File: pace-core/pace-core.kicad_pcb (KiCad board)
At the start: 4 copper layers, 100 x 80.1 mm, 174 parts, among them CN1 XT60PW-M, CN2 SMTSOM330BTR, CN3 SMTSOM330BTR, CN4 SMTSOM330BTR, CN5 SMTSOM330BTR, CN6 SMTSOM330BTR, CN7 SMTSOM330BTR, J1 MotorOut, J2 Wiz5500-Coprocessor-BoB, J4 Conn_02x05_Odd_Even, Q1 BSS138, Q10 ISC0802NLSATMA1, Q11 ISC0802NLSATMA1, Q12 ISC0802NLSATMA1, Q2 BSS138, Q3 BSS138, Q7 ISC0802NLSATMA1, Q8 ISC0802NLSATMA1, Q9 ISC0802NLSATMA1, SW1 SKRPACE010, SW2 SKRPACE010, SW3 DPDT, U1 ESP32-S3-WROOM-1, U10 LM75ADP,118, U11 LM75ADP,118, U12 SM06B-SRSS-TB, U13 SM06B-SRSS-TB, U2 DRV8353SRTAT, U3 USBLC6-2P6, U4 ADUM3160BRWZ-RL, U5 AMS1117-3.3, U6 XL7015E1, U7 REF35160QDBVR, U8 LM75ADP,118, U9 LM75ADP,118

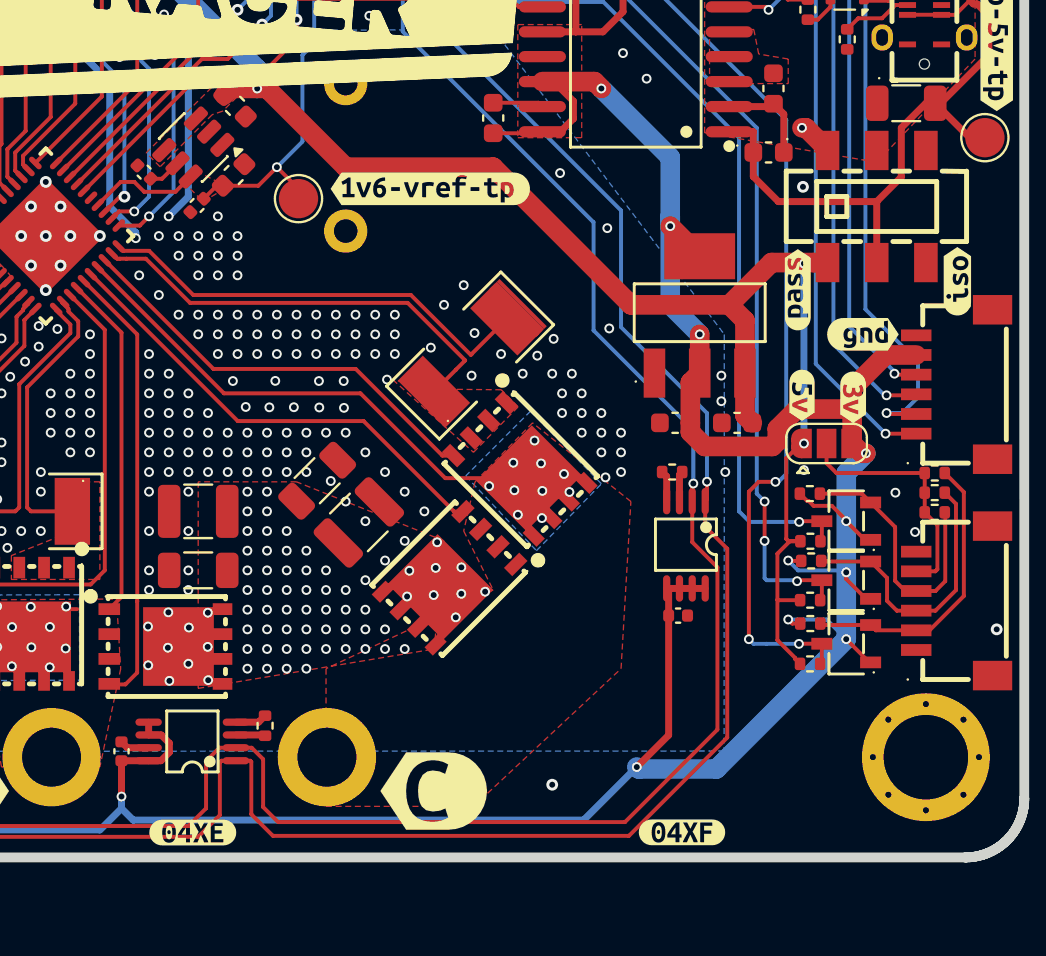
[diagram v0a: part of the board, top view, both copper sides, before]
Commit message: update connectors schematic and PCB layout, refresh r2 STEP export
Co-Authored-By: Claude Fable 5 <noreply@anthropic.com>
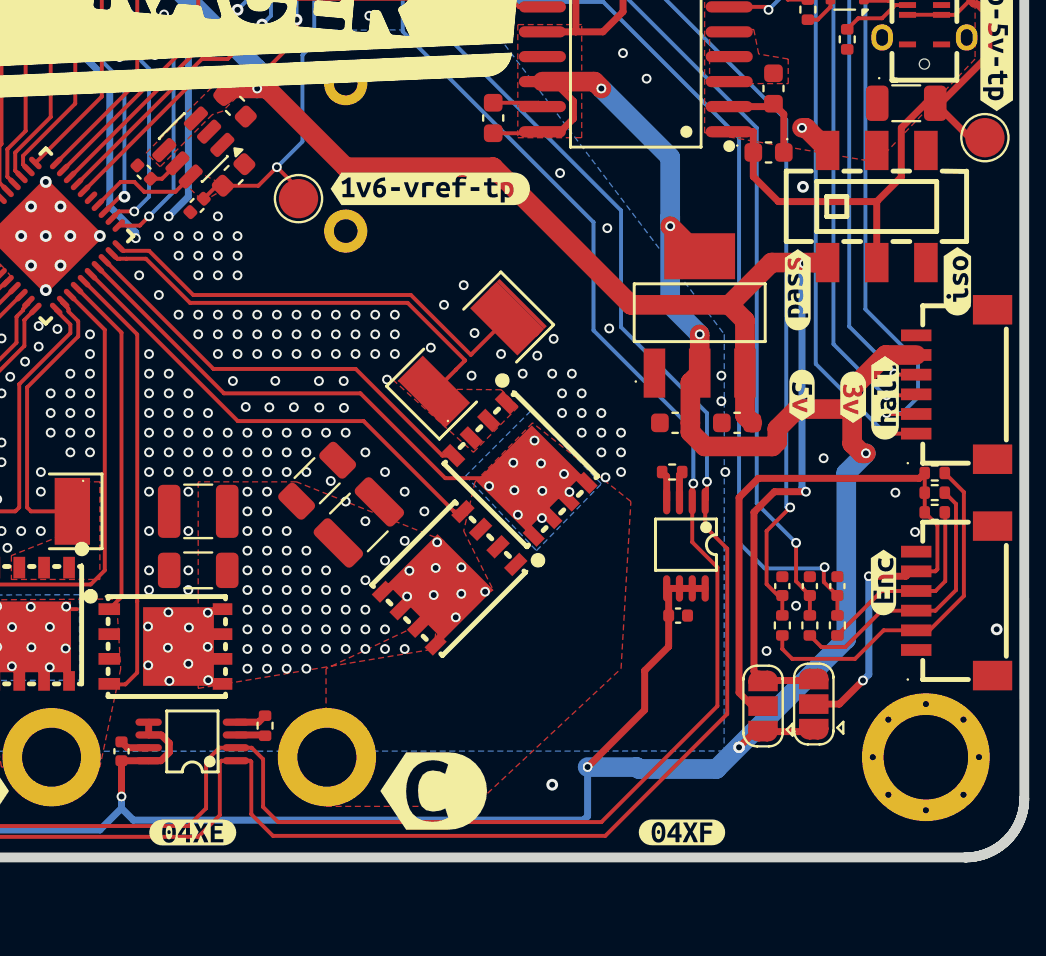
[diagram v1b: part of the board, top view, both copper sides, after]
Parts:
- removed Q1, Q2, Q3: BSS138, specific-parts-lib:SOT-23-3_L2.9-W1.6-P1.90-LS2.8-BR
- removed R41, R42, R43: 10k, Resistor_SMD:R_0402_1005Metric
- removed kibuzzard-6A76AD7E: G***, kibuzzard-6A76AD7E
- added C40: 1nF, Capacitor_SMD:C_0402_1005Metric, F.Cu at (187.7, 116.3)
- added C41: 1nF, Capacitor_SMD:C_0402_1005Metric, F.Cu at (189.1, 116.3)
- added C42: 1nF, Capacitor_SMD:C_0402_1005Metric, F.Cu at (190.5, 116.3)
- added JP5: SolderJumper_3_Bridged12, Jumper:SolderJumper-3_P1.3mm_Open_RoundedPad1.0x1.5mm, F.Cu at (186.7, 122.4)
- added kibuzzard-6A79703A: G***, kibuzzard-6A79703A, F.Cu at (192.8, 116.1)
- added kibuzzard-6A797050: G***, kibuzzard-6A797050, F.Cu at (192.9, 106.7)
- R25, R33, R34: value 10k -> 100R
- moved JP4 13.3 mm to (189.3, 122.3), turned to 90 degrees
- moved R34 4.50 mm to (190.5, 118.3), turned to -90 degrees
- moved R25 2.41 mm to (187.7, 118.3), turned to -90 degrees
- moved R33 1.28 mm to (189.1, 118.3), turned to -90 degrees
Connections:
- JP4 pad 1: +5V -> +3V3
- JP4 pad 2: /Connectors/v_pullup -> /Connectors/v_halls_pwr
- JP4 pad 3: +3V3 -> +5V
- R18 pad 1: Net-(Q1-S) -> Net-(R18-Pad1)
- R19 pad 1: Net-(Q2-S) -> Net-(R19-Pad1)
- R20 pad 1: Net-(Q3-S) -> Net-(R20-Pad1)
- R25 pad 2: +5V -> Net-(R18-Pad1)
- R33 pad 2: +5V -> Net-(R19-Pad1)
- R34 pad 2: +5V -> Net-(R20-Pad1)
- U13 pad 2: Net-(Q1-S) -> Net-(R18-Pad1)
- U13 pad 3: Net-(Q2-S) -> Net-(R19-Pad1)
- U13 pad 4: Net-(Q3-S) -> Net-(R20-Pad1)
- U13 pad 5: /Connectors/v_pullup -> /Connectors/v_halls_pwr
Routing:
- net Net-(R18-Pad1): track 0.00 -> 18.1 mm
- net /Connectors/v_pullup: track 12.5 -> 27.7 mm
- net Net-(Q1-S): track 14.8 -> 0.00 mm
- net Net-(Q2-S): track 14.2 -> 0.00 mm
- net Net-(R19-Pad1): track 0.00 -> 14.1 mm
- net Net-(Q3-S): track 13.7 -> 0.00 mm
- net /Connectors/v_halls_pwr: track 0.00 -> 10.6 mm, vias 0 -> 2
- net Net-(R20-Pad1): track 0.00 -> 10.1 mm
- net +3V3: track 332.5 -> 322.9 mm, vias 21 -> 17
- net C-Halls: track 67.3 -> 61.0 mm, vias 4 -> 2
- net A-halls: track 60.0 -> 63.8 mm
- net +5V: track 129.3 -> 131.7 mm
- net B-Halls: track 61.7 -> 60.7 mm, vias 4 -> 2
- net i2c-SDA: track 172.8 -> 172.1 mm
- net i2c-SCL: track 180.1 -> 179.4 mm
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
